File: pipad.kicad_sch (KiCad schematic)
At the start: 2 parts, among them J3 Conn_02x20_Odd_Even, J5 Conn_01x03

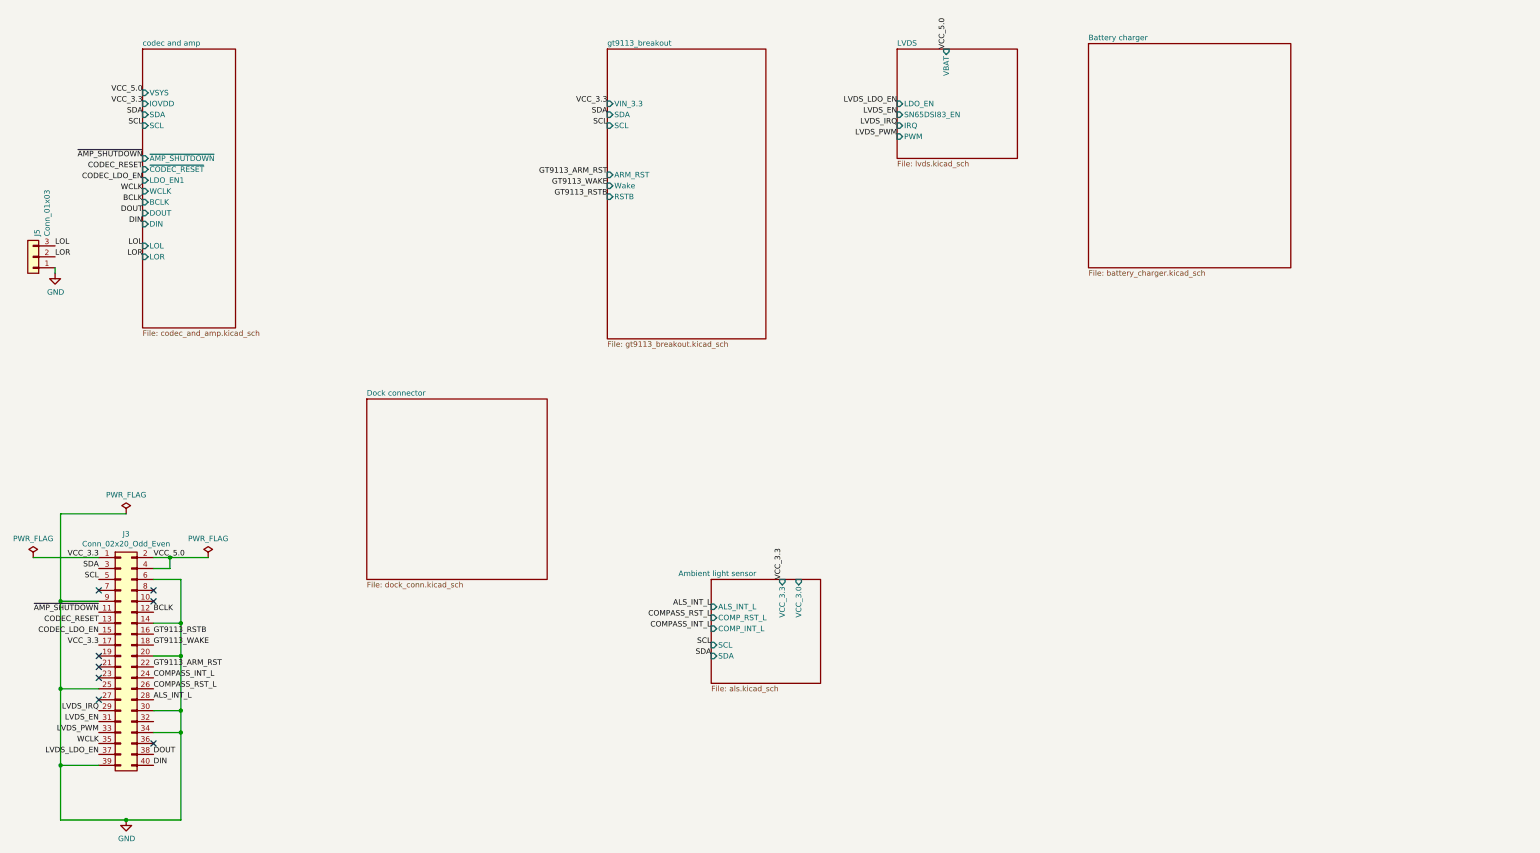
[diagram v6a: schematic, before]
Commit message: Add pinouts for dock connector; rearrange LCD backlight driver; copy the bq25895 schematic from SuperPower-RPi and add schottky to support 3.1A output on PMID.
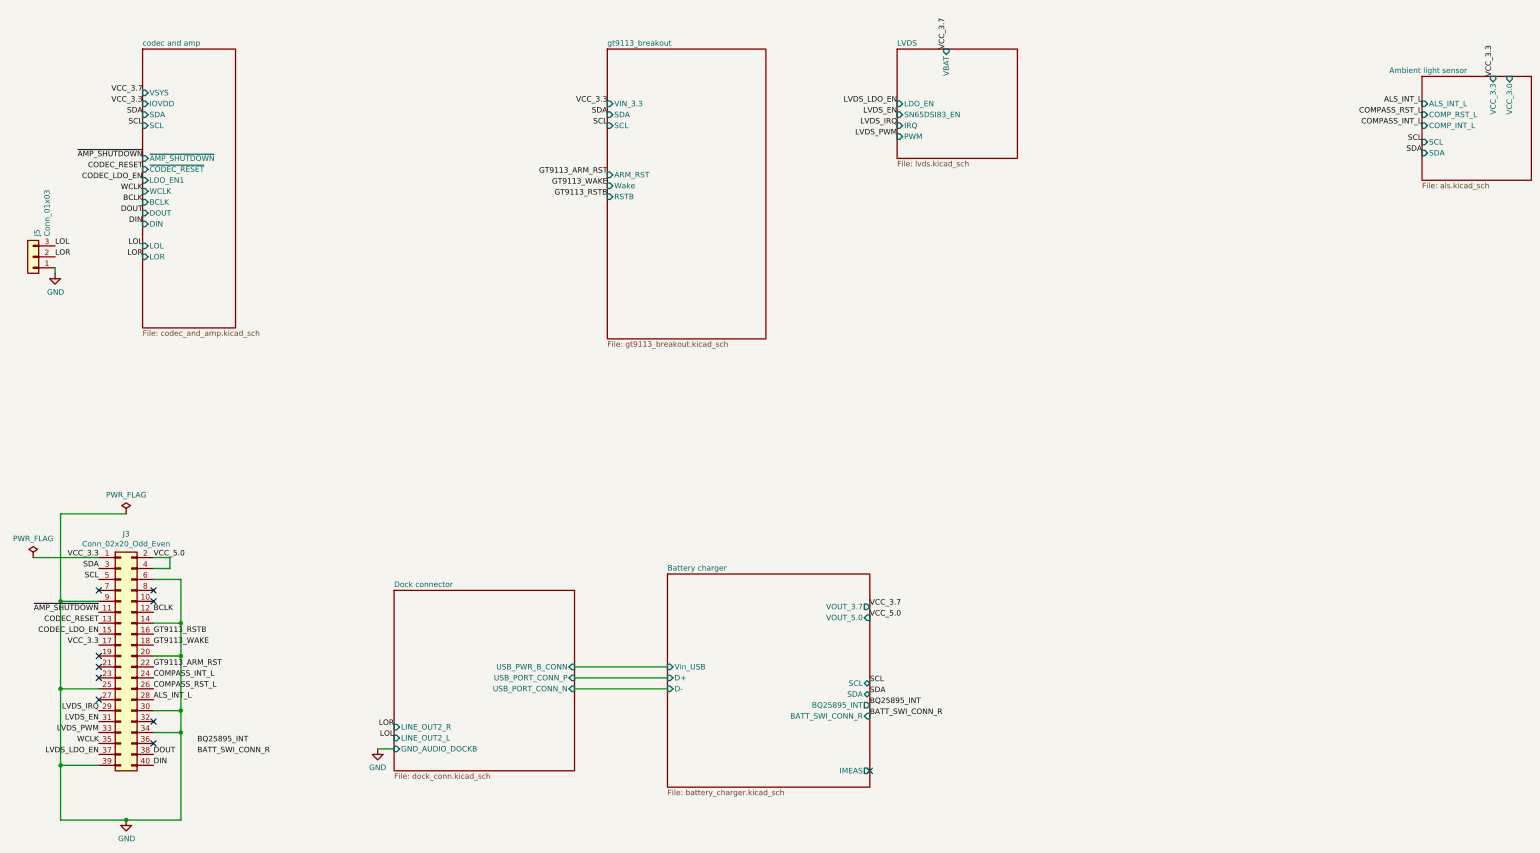
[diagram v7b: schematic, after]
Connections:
- no-connect marks 8 -> 10
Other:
- sheet Battery charger ports: added BATT_SWI_CONN_R, BQ25895_INT, D+, D-, IMEAS, SCL, SDA, VOUT_3.7, VOUT_5.0, Vin_USB; removed none
- sheet Dock connector ports: added GND_AUDIO_DOCKB, LINE_OUT2_L, LINE_OUT2_R, USB_PORT_CONN_N, USB_PORT_CONN_P, USB_PWR_B_CONN; removed none

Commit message: Wire more things up, move charger around.
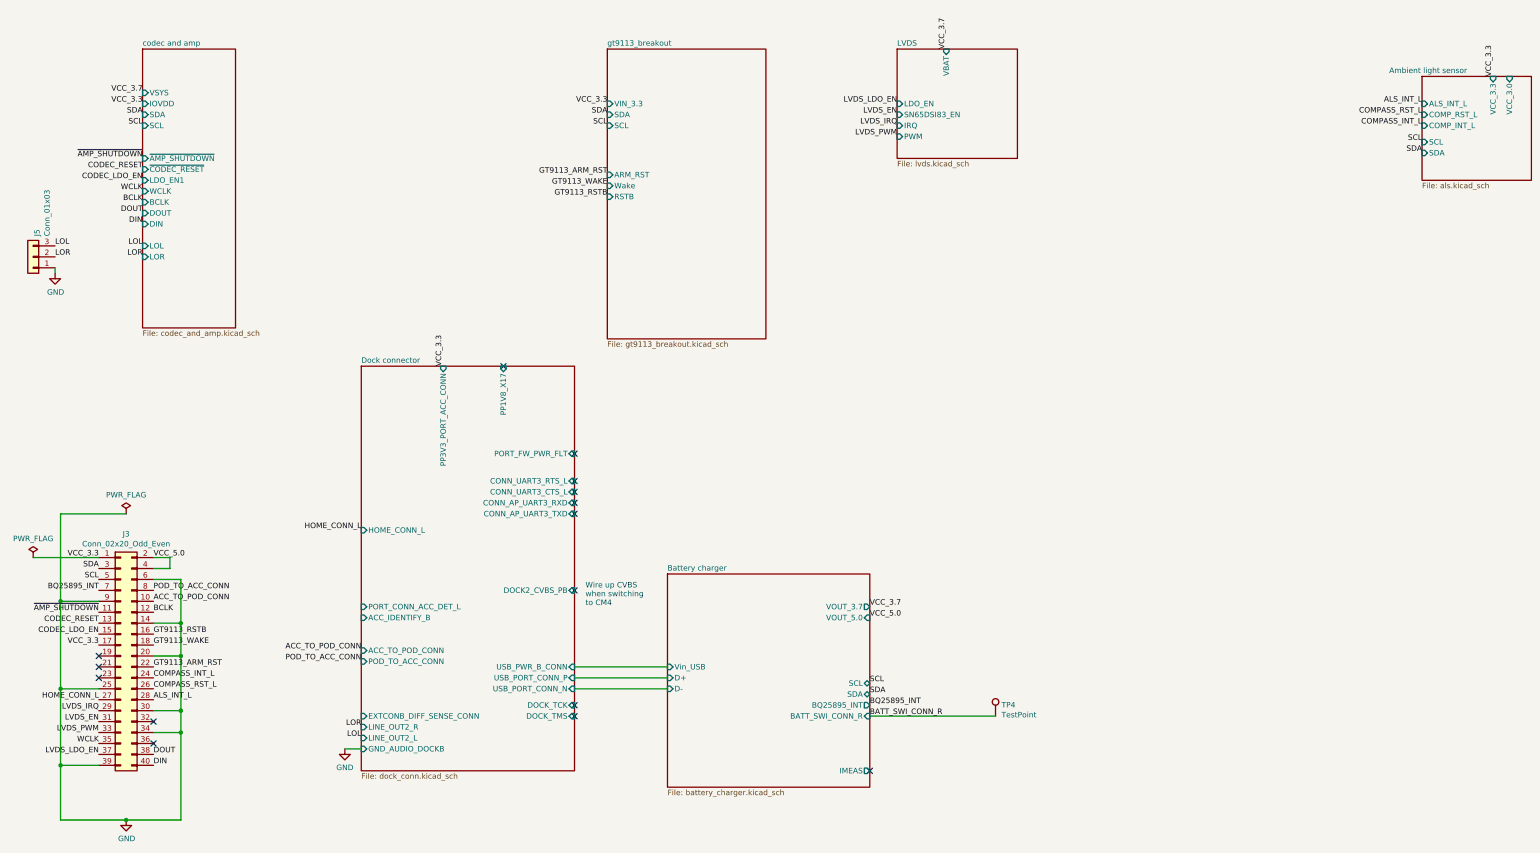
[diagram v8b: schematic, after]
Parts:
- added TP4: TestPoint, symbol Connector:TestPoint
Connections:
- net BATT_SWI_CONN_R: now also TP4.1
- net BQ25895_INT: now also J3.7 (Pin_7)
- net ACC_TO_POD_CONN: now reaches J3.10 (Pin_10)
- net HOME_CONN_L: now reaches J3.27 (Pin_27)
- net POD_TO_ACC_CONN: now reaches J3.8 (Pin_8)
- no-connect marks 10 -> 15
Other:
- sheet Dock connector ports: added ACC_IDENTIFY_B, ACC_TO_POD_CONN, CONN_AP_UART3_RXD, CONN_AP_UART3_TXD, CONN_UART3_CTS_L, CONN_UART3_RTS_L, DOCK2_CVBS_PB, DOCK_TCK, DOCK_TMS, EXTCONB_DIFF_SENSE_CONN, HOME_CONN_L, POD_TO_ACC_CONN, PORT_CONN_ACC_DET_L, PORT_FW_PWR_FLT, PP1V8_X17, PP3V3_PORT_ACC_CONN; removed none
- note added: "Wire up CVBS when switching to CM4"
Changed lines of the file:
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@@
   (junction (at 68.58 191.77) (diameter 1.016) (color 0 0 0 0))
   (junction (at 68.58 196.85) (diameter 1.016) (color 0 0 0 0))
-  (no_connect (at 49.53 163.83))
   (no_connect (at 49.53 179.07))
   (no_connect (at 49.53 181.61))
   (no_connect (at 49.53 184.15))
-  (no_connect (at 49.53 189.23))
-  (no_connect (at 62.23 163.83))
-  (no_connect (at 62.23 166.37))
   (no_connect (at 62.23 194.31))
   (no_connect (at 62.23 199.39))
+  (no_connect (at 143.51 111.76))
+  (no_connect (at 160.02 132.08))
+  (no_connect (at 160.02 138.43))
+  (no_connect (at 160.02 140.97))
+  (no_connect (at 160.02 143.51))
+  (no_connect (at 160.02 146.05))
+  (no_connect (at 160.02 163.83))
+  (no_connect (at 160.02 190.5))
+  (no_connect (at 160.02 193.04))
   (no_connect (at 228.6 205.74))
   (wire (pts (xy 34.29 156.21) (xy 49.53 156.21))
@@
     (stroke (width 0) (type solid) (color 0 0 0 0))
   )
-  (wire (pts (xy 114.3 200.66) (xy 118.11 200.66))
+  (wire (pts (xy 106.68 200.66) (xy 110.49 200.66))
     (stroke (width 0) (type solid) (color 0 0 0 0))
   )
@@
     (stroke (width 0) (type solid) (color 0 0 0 0))
   )
+  (wire (pts (xy 228.6 193.04) (xy 257.81 193.04))
+    (stroke (width 0) (type solid) (color 0 0 0 0))
+  )
+  (text "Wire up CVBS\nwhen switching\nto CM4" (at 162.56 167.64 0)
+    (effects (font (size 1.27 1.27)) (justify left bottom))
+  )
   (label "LOL" (at 39.37 83.82 0)
     (effects (font (size 1.27 1.27)) (justify left bottom))
@@
     (effects (font (size 1.27 1.27)) (justify right bottom))
   )
+  (label "BQ25895_INT" (at 49.53 163.83 180)
+    (effects (font (size 1.27 1.27)) (justify right bottom))
+  )
   (label "~AMP_SHUTDOWN" (at 49.53 168.91 180)
     (effects (font (size 1.27 1.27)) (justify right bottom))
@@
     (effects (font (size 1.27 1.27)) (justify right bottom))
   )
+  (label "HOME_CONN_L" (at 49.53 189.23 180)
+    (effects (font (size 1.27 1.27)) (justify right bottom))
+  )
   (label "LVDS_IRQ" (at 49.53 191.77 180)
     (effects (font (size 1.27 1.27)) (justify right bottom))
@@
     (effects (font (size 1.27 1.27)) (justify left bottom))
   )
+  (label "POD_TO_ACC_CONN" (at 62.23 163.83 0)
+    (effects (font (size 1.27 1.27)) (justify left bottom))
+  )
+  (label "ACC_TO_POD_CONN" (at 62.23 166.37 0)
+    (effects (font (size 1.27 1.27)) (justify left bottom))
+  )
   (label "BCLK" (at 62.23 168.91 0)
     (effects (font (size 1.27 1.27)) (justify left bottom))
@@
     (effects (font (size 1.27 1.27)) (justify left bottom))
   )
-  (label "BQ25895_INT" (at 72.39 199.39 0)
-    (effects (font (size 1.27 1.27)) (justify left bottom))
-  )
-  (label "BATT_SWI_CONN_R" (at 72.39 201.93 0)
-    (effects (font (size 1.27 1.27)) (justify left bottom))
-  )
-  (label "LOR" (at 118.11 195.58 180)
-    (effects (font (size 1.27 1.27)) (justify right bottom))
-  )
-  (label "LOL" (at 118.11 198.12 180)
-    (effects (font (size 1.27 1.27)) (justify right bottom))
+  (label "HOME_CONN_L" (at 110.49 149.86 180)
+    (effects (font (size 1.27 1.27)) (justify right bottom))
+  )
+  (label "ACC_TO_POD_CONN" (at 110.49 177.8 180)
+    (effects (font (size 1.27 1.27)) (justify right bottom))
+  )
+  (label "POD_TO_ACC_CONN" (at 110.49 180.34 180)
+    (effects (font (size 1.27 1.27)) (justify right bottom))
+  )
+  (label "LOR" (at 110.49 195.58 180)
+    (effects (font (size 1.27 1.27)) (justify right bottom))
+  )
+  (label "LOL" (at 110.49 198.12 180)
+    (effects (font (size 1.27 1.27)) (justify right bottom))
+  )
+  (label "VCC_3.3" (at 129.54 111.76 90)
+    (effects (font (size 1.27 1.27)) (justify left bottom))
   )
   (label "VCC_3.3" (at 167.64 50.8 180)
@@
     (pin "1")
   )
+  (symbol (lib_id "Connector:TestPoint") (at 257.81 193.04 0) (unit 1)
+    (in_bom yes) (on_board yes) (fields_autoplaced)
+    (property "Reference" "TP4" (id 0) (at 259.2071 190.4376 0)
+      (effects (font (size 1.27 1.27)) (justify left))
+    )
+    (property "Value" "TestPoint" (id 1) (at 259.2071 192.7363 0)
+      (effects (font (size 1.27 1.27)) (justify left))
+    )
+    (property "Footprint" "" (id 2) (at 262.89 193.04 0)
+      (effects (font (size 1.27 1.27)) hide)
+    )
+    (property "Datasheet" "~" (id 3) (at 262.89 193.04 0)
+      (effects (font (size 1.27 1.27)) hide)
+    )
+    (pin "1")
+  )
   (symbol (lib_id "power:GND") (at 39.37 90.17 0) (unit 1)
     (in_bom yes) (on_board yes)
@@
     (pin "1")
   )
-  (symbol (lib_id "power:GND") (at 114.3 200.66 0) (unit 1)
+  (symbol (lib_id "power:GND") (at 106.68 200.66 0) (unit 1)
     (in_bom yes) (on_board yes) (fields_autoplaced)
-    (property "Reference" "#PWR036" (id 0) (at 114.3 207.01 0)
-      (effects (font (size 1.27 1.27)) hide)
-    )
-    (property "Value" "GND" (id 1) (at 114.3 204.9844 0))
-    (property "Footprint" "" (id 2) (at 114.3 200.66 0)
-      (effects (font (size 1.27 1.27)) hide)
-    )
-    (property "Datasheet" "" (id 3) (at 114.3 200.66 0)
+    (property "Reference" "#PWR036" (id 0) (at 106.68 207.01 0)
+      (effects (font (size 1.27 1.27)) hide)
+    )
+    (property "Value" "GND" (id 1) (at 106.68 204.9844 0))
+    (property "Footprint" "" (id 2) (at 106.68 200.66 0)
+      (effects (font (size 1.27 1.27)) hide)
+    )
+    (property "Datasheet" "" (id 3) (at 106.68 200.66 0)
       (effects (font (size 1.27 1.27)) hide)
     )
@@
     )
   )
-  (sheet (at 118.11 163.83) (size 41.91 41.91) (fields_autoplaced)
+  (sheet (at 110.49 111.76) (size 49.53 93.98) (fields_autoplaced)
     (stroke (width 0.0006) (type solid) (color 0 0 0 0))
     (fill (color 0 0 0 0.0000))
-    (property "Sheet name" "Dock connector" (id 0) (at 118.11 163.1943 0)
+    (property "Sheet name" "Dock connector" (id 0) (at 110.49 111.1243 0)
       (effects (font (size 1.27 1.27)) (justify left bottom))
     )
-    (property "Sheet file" "dock_conn.kicad_sch" (id 1) (at 118.11 206.2487 0)
+    (property "Sheet file" "dock_conn.kicad_sch" (id 1) (at 110.49 206.2487 0)
       (effects (font (size 1.27 1.27)) (justify left top))
     )
@@
       (effects (font (size 1.27 1.27)) (justify right))
     )
-    (pin "LINE_OUT2_R" input (at 118.11 195.58 180)
-      (effects (font (size 1.27 1.27)) (justify left))
-    )
-    (pin "GND_AUDIO_DOCKB" input (at 118.11 200.66 180)
-      (effects (font (size 1.27 1.27)) (justify left))
-    )
-    (pin "LINE_OUT2_L" input (at 118.11 198.12 180)
+    (pin "LINE_OUT2_R" input (at 110.49 195.58 180)
+      (effects (font (size 1.27 1.27)) (justify left))
+    )
+    (pin "GND_AUDIO_DOCKB" input (at 110.49 200.66 180)
+      (effects (font (size 1.27 1.27)) (justify left))
+    )
+    (pin "LINE_OUT2_L" input (at 110.49 198.12 180)
       (effects (font (size 1.27 1.27)) (justify left))
     )
@@
     )
     (pin "USB_PORT_CONN_P" input (at 160.02 184.15 0)
+      (effects (font (size 1.27 1.27)) (justify right))
+    )
+    (pin "CONN_UART3_RTS_L" input (at 160.02 138.43 0)
+      (effects (font (size 1.27 1.27)) (justify right))
+    )
+    (pin "CONN_UART3_CTS_L" input (at 160.02 140.97 0)
+      (effects (font (size 1.27 1.27)) (justify right))
+    )
+    (pin "CONN_AP_UART3_RXD" input (at 160.02 143.51 0)
+      (effects (font (size 1.27 1.27)) (justify right))
+    )
+    (pin "PP1V8_X17" input (at 143.51 111.76 90)
+      (effects (font (size 1.27 1.27)) (justify right))
+    )
+    (pin "EXTCONB_DIFF_SENSE_CONN" input (at 110.49 193.04 180)
+      (effects (font (size 1.27 1.27)) (justify left))
+    )
+    (pin "CONN_AP_UART3_TXD" input (at 160.02 146.05 0)
+      (effects (font (size 1.27 1.27)) (justify right))
+    )
+    (pin "PORT_CONN_ACC_DET_L" input (at 110.49 167.64 180)
+      (effects (font (size 1.27 1.27)) (justify left))
+    )
+    (pin "ACC_IDENTIFY_B" input (at 110.49 170.18 180)
+      (effects (font (size 1.27 1.27)) (justify left))
+    )
+    (pin "PP3V3_PORT_ACC_CONN" input (at 129.54 111.76 90)
+      (effects (font (size 1.27 1.27)) (justify right))
+    )
+    (pin "PORT_FW_PWR_FLT" input (at 160.02 132.08 0)
+      (effects (font (size 1.27 1.27)) (justify right))
+    )
+    (pin "HOME_CONN_L" input (at 110.49 149.86 180)
+      (effects (font (size 1.27 1.27)) (justify left))
+    )
+    (pin "DOCK2_CVBS_PB" input (at 160.02 163.83 0)
+      (effects (font (size 1.27 1.27)) (justify right))
+    )
+    (pin "POD_TO_ACC_CONN" input (at 110.49 180.34 180)
+      (effects (font (size 1.27 1.27)) (justify left))
+    )
+    (pin "DOCK_TCK" input (at 160.02 190.5 0)
+      (effects (font (size 1.27 1.27)) (justify right))
+    )
+    (pin "ACC_TO_POD_CONN" input (at 110.49 177.8 180)
+      (effects (font (size 1.27 1.27)) (justify left))
+    )
+    (pin "DOCK_TMS" input (at 160.02 193.04 0)
       (effects (font (size 1.27 1.27)) (justify right))
     )
@@
       (reference "J5") (unit 1) (value "Conn_01x03") (footprint "Connector_PinHeader_2.54mm:PinHeader_1x03_P2.54mm_Vertical")
     )
+    (path "/ffb64783-aa4c-484c-887c-79ad41f72096"
+      (reference "TP4") (unit 1) (value "TestPoint") (footprint "")
+    )
     (path "/00000000-0000-0000-0000-00006026a3be/00000000-0000-0000-0000-000060293f25"
